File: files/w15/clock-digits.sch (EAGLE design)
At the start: 6 parts, among them IC1 ATTINY44-SSU, IC2 5V

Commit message: board routing
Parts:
- added R10, R11, R12, R13, R14, R15, R2, R3, R4, R5, R6, R7, R8, R9: (no value), fab:RES-US1206FAB
- added U$10, U$11, U$12, U$13, U$14, U$15, U$16, U$3, U$4, U$5, U$6, U$7, U$8, U$9: LEDFAB1206, fab:LEDFAB1206
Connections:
- new net N$1: IC1.(PCINT0/AREF/ADC0)PA0, R2.1, R9.1
- new net N$10: R6.1, U$11.A
- new net N$11: IC1.(PCINT8/XTAL1/CLKI)PB0, R14.2, R7.2
- new net N$12: R7.1, U$12.A
- new net N$14: R8.1, U$6.A
- new net N$15: IC1.(PCINT10/INT0/OC0A/CKOUT)PB2, R15.2, U$10.C, U$11.C, U$12.C, U$3.C, U$4.C, U$5.C, U$6.C
- new net N$16: R9.2, U$7.A
- new net N$17: R15.1, U$16.A
- new net N$18: R10.1, U$8.A
- new net N$2: R2.2, U$3.A
- new net N$20: R11.1, U$9.A
- new net N$21: R12.1, U$13.A
- new net N$23: R13.1, U$14.A
- new net N$24: R14.1, U$15.A
- new net N$28: IC1.(PCINT9/XTAL2)PB1, R8.2, U$13.C, U$14.C, U$15.C, U$16.C, U$7.C, U$8.C, U$9.C
- new net N$3: IC1.(PCINT1/AIN0/ADC1)PA1, R10.2, R3.2
- new net N$4: R3.1, U$4.A
- new net N$5: IC1.(PCINT2/AIN1/ADC2)PA2, R11.2, R4.2
- new net N$6: R4.1, U$5.A
- new net N$7: IC1.(PCINT3/T0/ADC3)PA3, R12.2, R5.2
- new net N$8: R5.1, U$10.A
- new net N$9: IC1.(PCINT7/ICP/OC0B/ADC7)PA7, R13.2, R6.2
- net SCK: now also IC1.(PCINT4/T1/SCL/USCK/ADC4)PA4

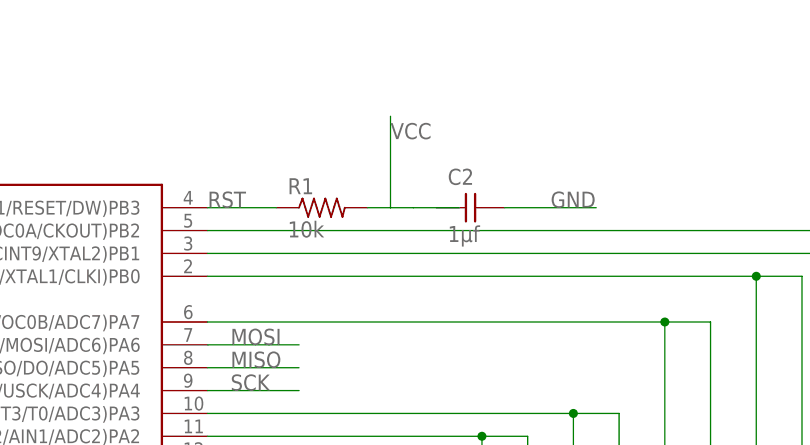
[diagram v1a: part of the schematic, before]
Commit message: first digit routed internally
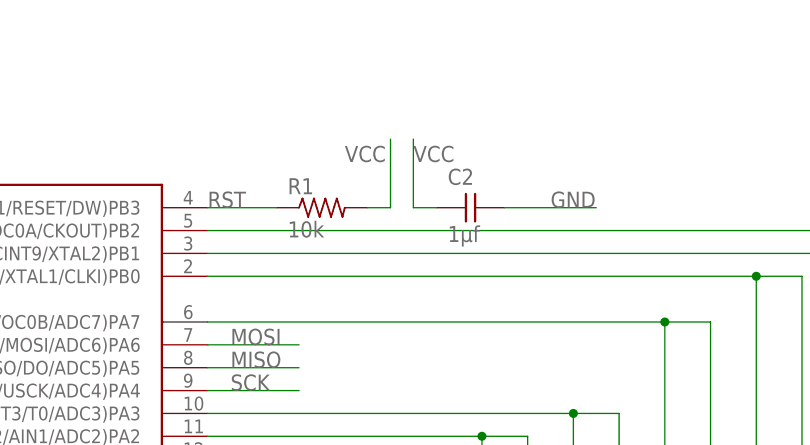
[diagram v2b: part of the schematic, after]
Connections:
- net VCC: now also C2.1
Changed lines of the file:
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@@
 </variantdefs>
 <classes>
-<class number="0" name="default" width="0.4826" drill="0">
+<class number="0" name="default" width="0.4572" drill="0">
 <clearance class="0" value="1.6256"/>
 </class>
@@
 </segment>
 <segment>
+<pinref part="C2" gate="&gt;NAME" pin="1"/>
+<wire x1="160.02" y1="71.12" x2="157.48" y2="71.12" width="0.1524" layer="91"/>
+<wire x1="157.48" y1="71.12" x2="157.48" y2="78.74" width="0.1524" layer="91"/>
+<label x="157.48" y="76.2" size="1.778" layer="95"/>
+</segment>
+<segment>
 <pinref part="R1" gate="G$1" pin="2"/>
 <wire x1="152.4" y1="71.12" x2="154.94" y2="71.12" width="0.1524" layer="91"/>
-<wire x1="157.48" y1="71.12" x2="162.56" y2="71.12" width="0.1524" layer="91"/>
-<wire x1="157.48" y1="71.12" x2="154.94" y2="71.12" width="0.1524" layer="91"/>
-<wire x1="154.94" y1="71.12" x2="154.94" y2="81.28" width="0.1524" layer="91"/>
-<label x="154.94" y="78.74" size="1.778" layer="95"/>
+<wire x1="154.94" y1="71.12" x2="154.94" y2="78.74" width="0.1524" layer="91"/>
+<label x="149.86" y="76.2" size="1.778" layer="95"/>
 </segment>
 </net>
